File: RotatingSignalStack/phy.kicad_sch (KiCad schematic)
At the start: 20 parts, among them U4 DP83825I

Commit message: Added everything
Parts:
- C15, C16, C17, C18, C22, C23, C24, C25, C26, C27, C28, C29: footprint (none) -> Capacitor_SMD:C_0603_1608Metric_Pad1.08x0.95mm_HandSolder
- FB1, FB4: footprint (none) -> SignalStack:BEADC0603X33N
- R11, R12, R13, R7, R8: footprint (none) -> Resistor_SMD:R_0603_1608Metric_Pad0.98x0.95mm_HandSolder
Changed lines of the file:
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@@
 			)
 		)
-		(property "Footprint" ""
+		(property "Footprint" "Capacitor_SMD:C_0603_1608Metric_Pad1.08x0.95mm_HandSolder"
 			(at 181.61 102.5652 0)
 			(effects
@@
 			)
 		)
-		(property "Footprint" ""
+		(property "Footprint" "Capacitor_SMD:C_0603_1608Metric_Pad1.08x0.95mm_HandSolder"
 			(at 137.4648 46.99 0)
 			(effects
@@
 			)
 		)
-		(property "Footprint" ""
+		(property "Footprint" "Capacitor_SMD:C_0603_1608Metric_Pad1.08x0.95mm_HandSolder"
 			(at 190.1952 54.61 0)
 			(effects
@@
 			)
 		)
-		(property "Footprint" ""
+		(property "Footprint" "Capacitor_SMD:C_0603_1608Metric_Pad1.08x0.95mm_HandSolder"
 			(at 181.61 89.8652 0)
 			(effects
@@
 			)
 		)
-		(property "Footprint" ""
+		(property "Footprint" "Capacitor_SMD:C_0603_1608Metric_Pad1.08x0.95mm_HandSolder"
 			(at 113.3348 46.99 0)
 			(effects
@@
 			)
 		)
-		(property "Footprint" ""
+		(property "Footprint" "Capacitor_SMD:C_0603_1608Metric_Pad1.08x0.95mm_HandSolder"
 			(at 181.61 115.2652 0)
 			(effects
@@
 			)
 		)
-		(property "Footprint" ""
+		(property "Footprint" "Resistor_SMD:R_0603_1608Metric_Pad0.98x0.95mm_HandSolder"
 			(at 92.964 113.284 90)
 			(effects
@@
 			)
 		)
-		(property "Footprint" ""
+		(property "Footprint" "Capacitor_SMD:C_0603_1608Metric_Pad1.08x0.95mm_HandSolder"
 			(at 181.61 77.1652 0)
 			(effects
@@
 			)
 		)
-		(property "Footprint" ""
+		(property "Footprint" "Resistor_SMD:R_0603_1608Metric_Pad0.98x0.95mm_HandSolder"
 			(at 92.964 128.524 90)
 			(effects
@@
 			)
 		)
-		(property "Footprint" ""
+		(property "Footprint" "SignalStack:BEADC0603X33N"
 			(at 191.008 40.64 90)
 			(effects
@@
 			)
 		)
-		(property "Footprint" ""
+		(property "Footprint" "Capacitor_SMD:C_0603_1608Metric_Pad1.08x0.95mm_HandSolder"
 			(at 154.6352 54.61 0)
 			(effects
@@
 			)
 		)
-		(property "Footprint" ""
+		(property "Footprint" "Resistor_SMD:R_0603_1608Metric_Pad0.98x0.95mm_HandSolder"
 			(at 176.276 130.556 90)
 			(effects
@@
 			)
 		)
-		(property "Footprint" ""
+		(property "Footprint" "Resistor_SMD:R_0603_1608Metric_Pad0.98x0.95mm_HandSolder"
 			(at 113.284 105.664 90)
 			(effects
@@
 			)
 		)
-		(property "Footprint" ""
+		(property "Footprint" "Resistor_SMD:R_0603_1608Metric_Pad0.98x0.95mm_HandSolder"
 			(at 92.964 141.224 90)
 			(effects
@@
 			)
 		)
-		(property "Footprint" ""
+		(property "Footprint" "Capacitor_SMD:C_0603_1608Metric_Pad1.08x0.95mm_HandSolder"
 			(at 166.0652 54.61 0)
 			(effects
@@
 			)
 		)
-		(property "Footprint" ""
+		(property "Footprint" "Capacitor_SMD:C_0603_1608Metric_Pad1.08x0.95mm_HandSolder"
 			(at 126.0348 46.99 0)
 			(effects
@@
 			)
 		)
-		(property "Footprint" ""
+		(property "Footprint" "Capacitor_SMD:C_0603_1608Metric_Pad1.08x0.95mm_HandSolder"
 			(at 101.9048 46.99 0)
 			(effects
@@
 			)
 		)
-		(property "Footprint" ""
+		(property "Footprint" "Capacitor_SMD:C_0603_1608Metric_Pad1.08x0.95mm_HandSolder"
 			(at 178.7652 54.61 0)
 			(effects
@@
 			)
 		)
-		(property "Footprint" ""
+		(property "Footprint" "SignalStack:BEADC0603X33N"
 			(at 104.648 40.64 90)
 			(effects

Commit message: placement fix
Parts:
- C17, C23: value 100nF -> 0.1uF

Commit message: more layout
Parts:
- C15, C16, C17, C18, C22, C23, C24, C25, C26, C27, C28, C29: footprint Capacitor_SMD:C_0603_1608Metric_Pad1.08x0.95mm_HandSolder -> Capacitor_SMD:C_0402_1005Metric_Pad0.74x0.62mm_HandSolder
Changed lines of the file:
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@@
 			)
 		)
-		(property "Footprint" "Capacitor_SMD:C_0603_1608Metric_Pad1.08x0.95mm_HandSolder"
+		(property "Footprint" "Capacitor_SMD:C_0402_1005Metric_Pad0.74x0.62mm_HandSolder"
 			(at 181.61 102.5652 0)
 			(effects
@@
 			)
 		)
-		(property "Footprint" "Capacitor_SMD:C_0603_1608Metric_Pad1.08x0.95mm_HandSolder"
+		(property "Footprint" "Capacitor_SMD:C_0402_1005Metric_Pad0.74x0.62mm_HandSolder"
 			(at 137.4648 46.99 0)
 			(effects
@@
 			)
 		)
-		(property "Footprint" "Capacitor_SMD:C_0603_1608Metric_Pad1.08x0.95mm_HandSolder"
+		(property "Footprint" "Capacitor_SMD:C_0402_1005Metric_Pad0.74x0.62mm_HandSolder"
 			(at 190.1952 54.61 0)
 			(effects
@@
 			)
 		)
-		(property "Footprint" "Capacitor_SMD:C_0603_1608Metric_Pad1.08x0.95mm_HandSolder"
+		(property "Footprint" "Capacitor_SMD:C_0402_1005Metric_Pad0.74x0.62mm_HandSolder"
 			(at 181.61 89.8652 0)
 			(effects
@@
 			)
 		)
-		(property "Footprint" "Capacitor_SMD:C_0603_1608Metric_Pad1.08x0.95mm_HandSolder"
+		(property "Footprint" "Capacitor_SMD:C_0402_1005Metric_Pad0.74x0.62mm_HandSolder"
 			(at 113.3348 46.99 0)
 			(effects
@@
 			)
 		)
-		(property "Footprint" "Capacitor_SMD:C_0603_1608Metric_Pad1.08x0.95mm_HandSolder"
+		(property "Footprint" "Capacitor_SMD:C_0402_1005Metric_Pad0.74x0.62mm_HandSolder"
 			(at 181.61 115.2652 0)
 			(effects
@@
 			)
 		)
-		(property "Footprint" "Capacitor_SMD:C_0603_1608Metric_Pad1.08x0.95mm_HandSolder"
+		(property "Footprint" "Capacitor_SMD:C_0402_1005Metric_Pad0.74x0.62mm_HandSolder"
 			(at 181.61 77.1652 0)
 			(effects
@@
 			)
 		)
-		(property "Footprint" "Capacitor_SMD:C_0603_1608Metric_Pad1.08x0.95mm_HandSolder"
+		(property "Footprint" "Capacitor_SMD:C_0402_1005Metric_Pad0.74x0.62mm_HandSolder"
 			(at 154.6352 54.61 0)
 			(effects
@@
 			)
 		)
-		(property "Footprint" "Capacitor_SMD:C_0603_1608Metric_Pad1.08x0.95mm_HandSolder"
+		(property "Footprint" "Capacitor_SMD:C_0402_1005Metric_Pad0.74x0.62mm_HandSolder"
 			(at 166.0652 54.61 0)
 			(effects
@@
 			)
 		)
-		(property "Footprint" "Capacitor_SMD:C_0603_1608Metric_Pad1.08x0.95mm_HandSolder"
+		(property "Footprint" "Capacitor_SMD:C_0402_1005Metric_Pad0.74x0.62mm_HandSolder"
 			(at 126.0348 46.99 0)
 			(effects
@@
 			)
 		)
-		(property "Footprint" "Capacitor_SMD:C_0603_1608Metric_Pad1.08x0.95mm_HandSolder"
+		(property "Footprint" "Capacitor_SMD:C_0402_1005Metric_Pad0.74x0.62mm_HandSolder"
 			(at 101.9048 46.99 0)
 			(effects
@@
 			)
 		)
-		(property "Footprint" "Capacitor_SMD:C_0603_1608Metric_Pad1.08x0.95mm_HandSolder"
+		(property "Footprint" "Capacitor_SMD:C_0402_1005Metric_Pad0.74x0.62mm_HandSolder"
 			(at 178.7652 54.61 0)
 			(effects

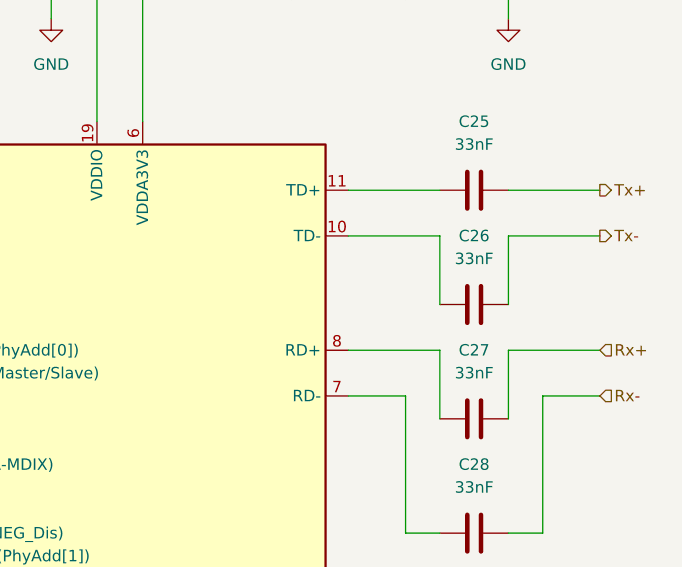
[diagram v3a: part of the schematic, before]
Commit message: Finished traces, added silkscreen
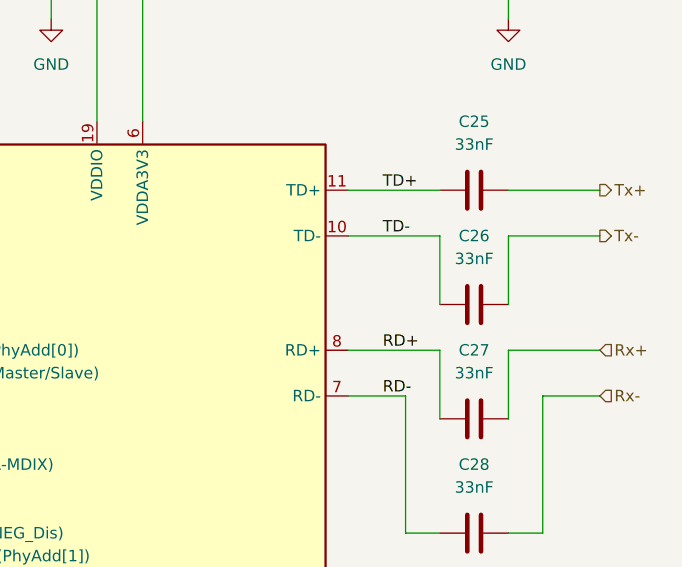
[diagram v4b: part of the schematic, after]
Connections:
- net RD+: now reaches C27.2, U4.8 (RD+)
- net TD-: now reaches C26.2, U4.10 (TD-)
- net RD-: now reaches C28.2, U4.7 (RD-)
- net TD+: now reaches C25.2, U4.11 (TD+)
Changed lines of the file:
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@@
+		)
+	)
+	(label "RD+"
+		(at 175.26 93.98 0)
+		(effects
+			(font
+				(size 1.27 1.27)
+			)
+			(justify left bottom)
+		)
+	)
+	(label "RD-"
+		(at 175.26 99.06 0)
+		(effects
+			(font
+				(size 1.27 1.27)
+			)
+			(justify left bottom)
+		)
+	)
+	(label "TD+"
+		(at 175.26 76.2 0)
+		(effects
+			(font
+				(size 1.27 1.27)
+			)
+			(justify left bottom)
+		)
+	)
+	(label "TD-"
+		(at 175.26 81.28 0)
+		(effects
+			(font
+				(size 1.27 1.27)
+			)
+			(justify left bottom)
 		)
 	)

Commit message: Added ground edges and fixed capacitors and layout issues
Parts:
- C25, C26, C27, C28: footprint Capacitor_SMD:C_0402_1005Metric_Pad0.74x0.62mm_HandSolder -> Capacitor_SMD:C_0603_1608Metric_Pad1.08x0.95mm_HandSolder
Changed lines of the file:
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@@
 			)
 		)
-		(property "Footprint" "Capacitor_SMD:C_0402_1005Metric_Pad0.74x0.62mm_HandSolder"
+		(property "Footprint" "Capacitor_SMD:C_0603_1608Metric_Pad1.08x0.95mm_HandSolder"
 			(at 181.61 102.5652 0)
 			(effects
@@
 			)
 		)
-		(property "Footprint" "Capacitor_SMD:C_0402_1005Metric_Pad0.74x0.62mm_HandSolder"
+		(property "Footprint" "Capacitor_SMD:C_0603_1608Metric_Pad1.08x0.95mm_HandSolder"
 			(at 181.61 89.8652 0)
 			(effects
@@
 			)
 		)
-		(property "Footprint" "Capacitor_SMD:C_0402_1005Metric_Pad0.74x0.62mm_HandSolder"
+		(property "Footprint" "Capacitor_SMD:C_0603_1608Metric_Pad1.08x0.95mm_HandSolder"
 			(at 181.61 115.2652 0)
 			(effects
@@
 			)
 		)
-		(property "Footprint" "Capacitor_SMD:C_0402_1005Metric_Pad0.74x0.62mm_HandSolder"
+		(property "Footprint" "Capacitor_SMD:C_0603_1608Metric_Pad1.08x0.95mm_HandSolder"
 			(at 181.61 77.1652 0)
 			(effects

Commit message: final layout
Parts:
- FB1, FB4: footprint SignalStack:BEADC0603X33N -> SignalStack:FB_MI0603L221R-10
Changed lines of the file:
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@@
 			)
 		)
-		(property "Footprint" "SignalStack:BEADC0603X33N"
+		(property "Footprint" "SignalStack:FB_MI0603L221R-10"
 			(at 191.008 40.64 90)
 			(effects
@@
 			)
 		)
-		(property "Footprint" "SignalStack:BEADC0603X33N"
+		(property "Footprint" "SignalStack:FB_MI0603L221R-10"
 			(at 104.648 40.64 90)
 			(effects
